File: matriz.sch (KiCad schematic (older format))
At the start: 69 parts

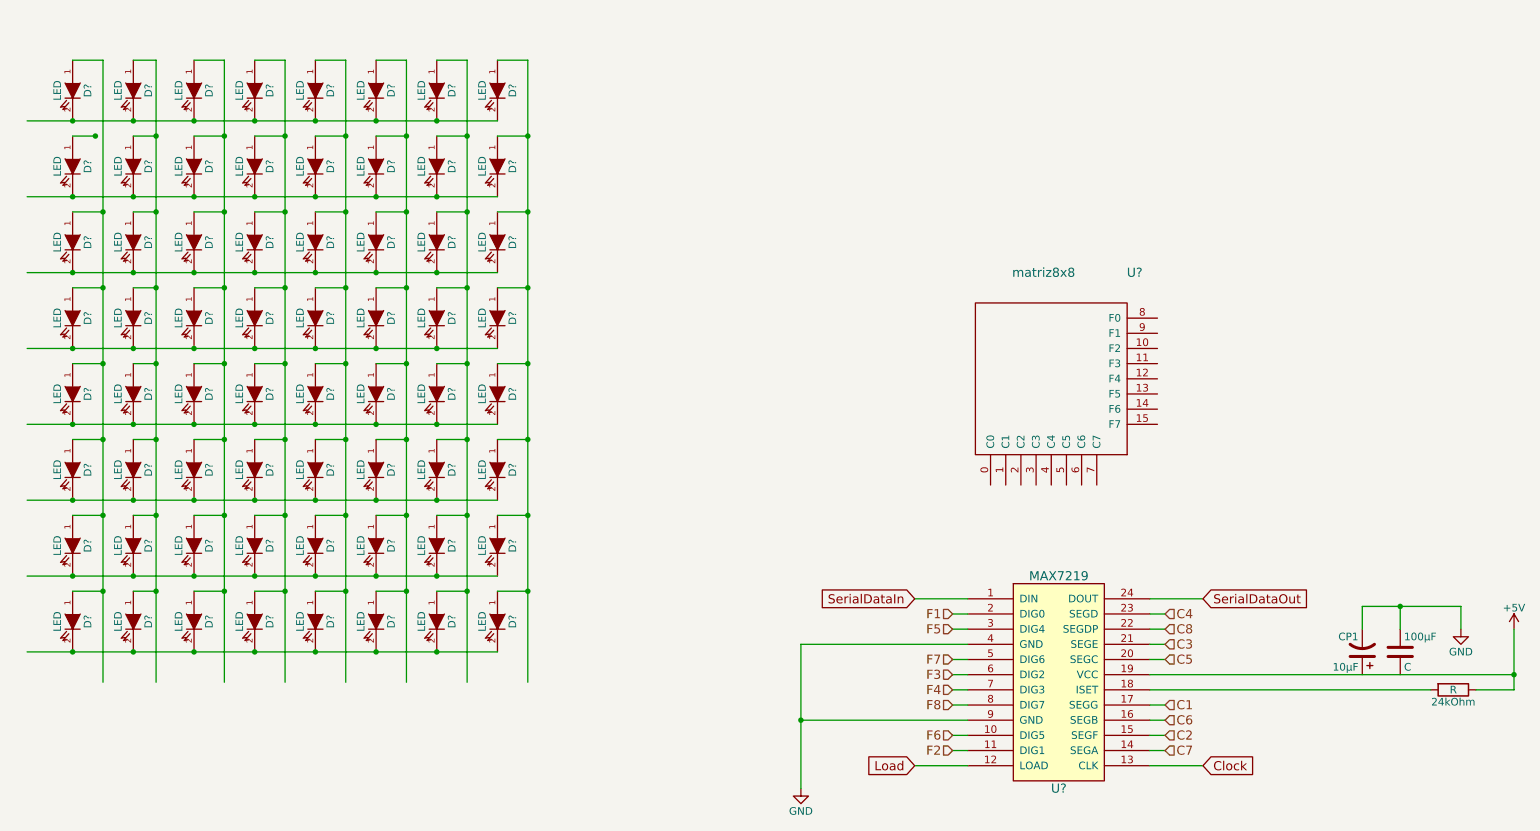
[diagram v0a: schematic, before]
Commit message: Actualizaciones importantes en el esquema y error unidad capacitor
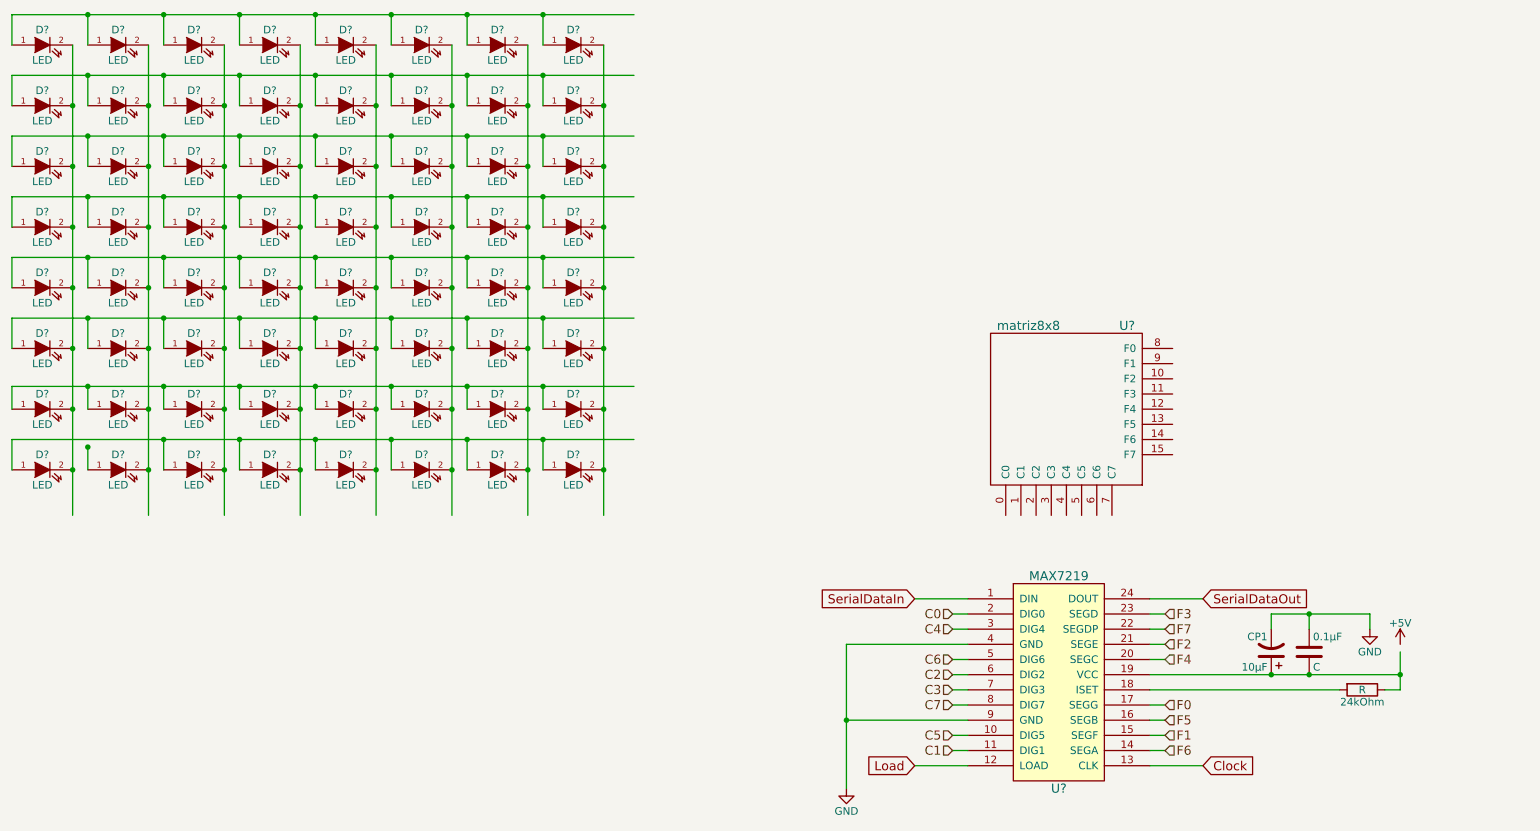
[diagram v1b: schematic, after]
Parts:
- removed U?: matriz8x8, symbol matriz8x8
- added U?: matriz8x8, symbol matriz8x8
- renumbered 100µF to 0.1µF
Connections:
- net labels added: C0, F0
- net labels removed: C8, F8
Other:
- moved on the sheet: 0.1µF, 10µF, 24kOhm, D?
